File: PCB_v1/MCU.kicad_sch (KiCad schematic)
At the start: 40 parts, among them J6 Conn_ARM_JTAG_SWD_10, SW9 SW_Push, U5 STM32F405RGTx, Y1 ASE-8MHz-L-C-T

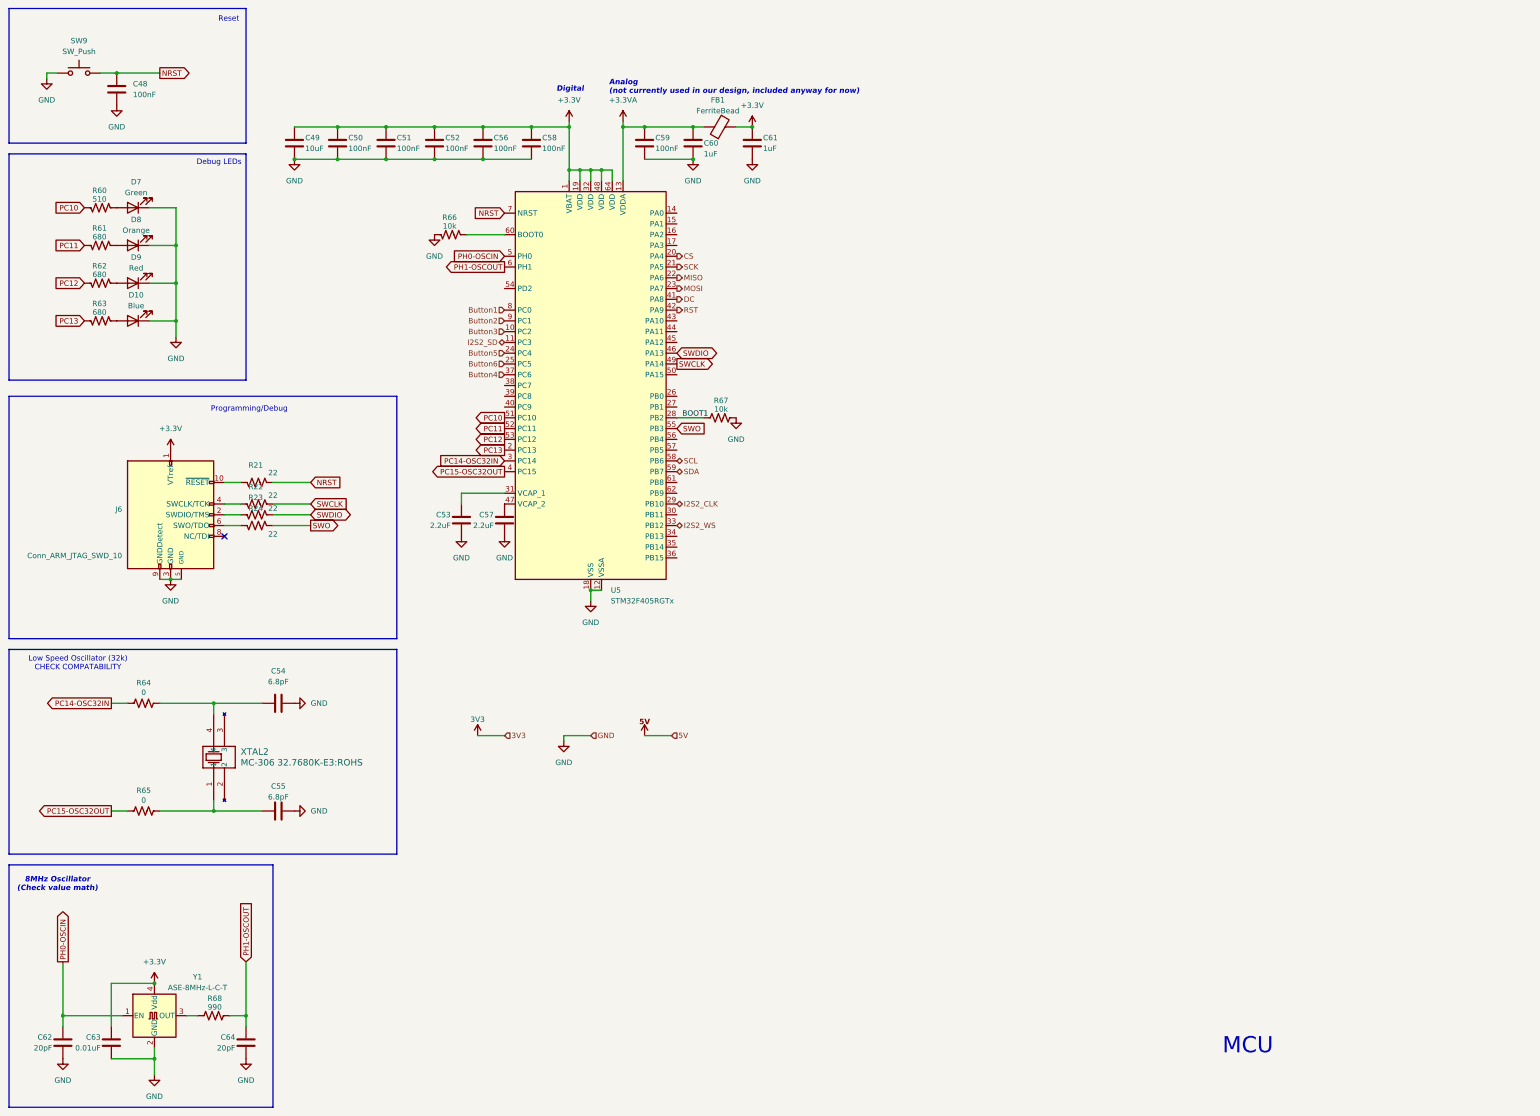
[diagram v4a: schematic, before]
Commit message: Update before adding AGND for the power delivery
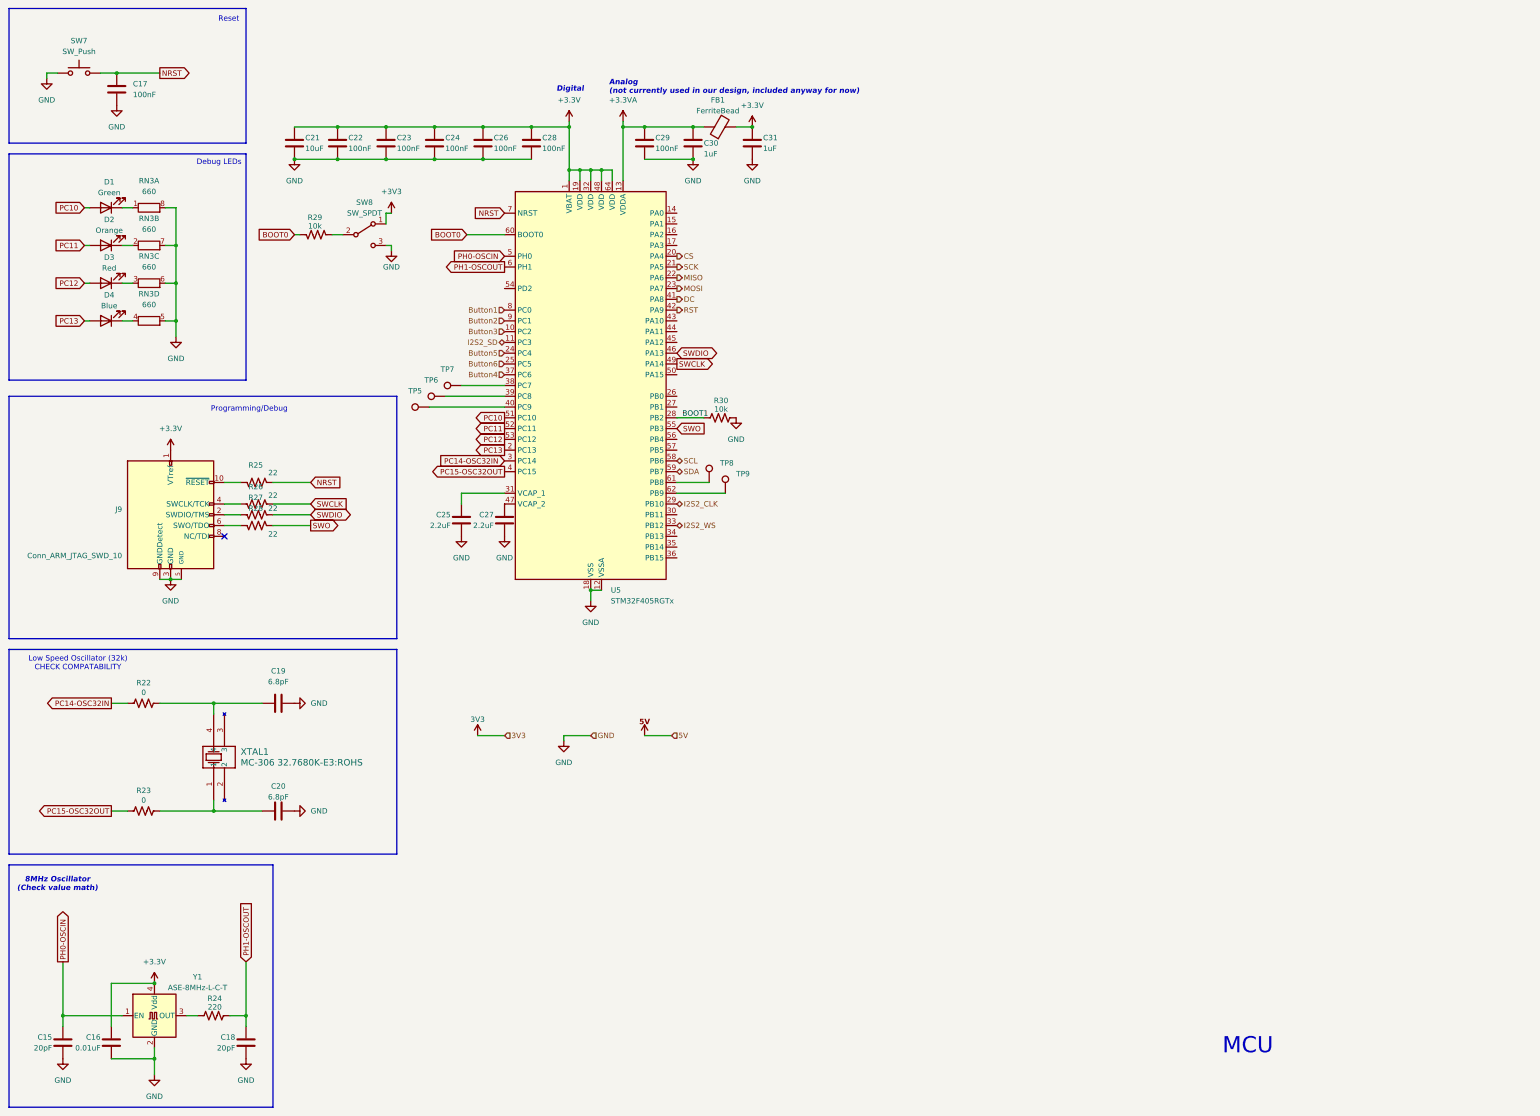
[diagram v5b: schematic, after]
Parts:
- removed R60: 510, Resistor_SMD:R_0805_2012Metric, symbol Device:R_US
- removed R61, R62, R63: 680, Resistor_SMD:R_0805_2012Metric, symbol Device:R_US
- removed R66: 10k, Resistor_SMD:R_0805_2012Metric, symbol Device:R_US
- added R29: 10k, Resistor_SMD:R_0805_2012Metric, symbol Device:R_US
- added RN3: 660, symbol Device:R_Pack04_Split
- added SW8: SW_SPDT, Button_Switch_SMD:SW_SPDT_PCM12, symbol Switch:SW_SPDT
- added TP5, TP6, TP7, TP8, TP9: ~, TestPoint:TestPoint_THTPad_D1.0mm_Drill0.5mm, symbol Connector:TestPoint
- R24: renamed from R68; value 990 -> 220
- renumbered C62 to C15, C63 to C16, C48 to C17, C64 to C18, C54 to C19, C55 to C20, C49 to C21, C50 to C22, C51 to C23, C52 to C24, C53 to C25, C56 to C26, C57 to C27, C58 to C28, C59 to C29, C60 to C30, C61 to C31, D7 to D1, D8 to D2, D9 to D3, D10 to D4, J6 to J9, R64 to R22, R65 to R23, R21 to R25, R22 to R26, R23 to R27, R24 to R28, R67 to R30, SW9 to SW7, XTAL2 to XTAL1
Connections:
- net GND: now also RN3.5 (R4.2), RN3.6 (R3.2), RN3.7 (R2.2), RN3.8 (R1.2), SW8.3 (C); no longer D1.1 (K), D2.1 (K), D3.1 (K), D4.1 (K)
- net PC10: now also D1.2 (A)
- net PC11: now also D2.2 (A)
- net PC12: now also D3.2 (A)
- net PC13: now also D4.2 (A)
- net BOOT0: now reaches U5.60 (BOOT0)
- net BOOT0: now also R29.2
- net at U5.38 (PC7): now also TP7.1
- net at U5.39 (PC8): now also TP6.1
- net at U5.40 (PC9): now also TP5.1
- net at U5.61 (PB8): now also TP8.1
- net at U5.62 (PB9): now also TP9.1
- new net: D3.1 (K), RN3.3 (R3.1)
- new net: D2.1 (K), RN3.2 (R2.1)
- new net: D1.1 (K), RN3.1 (R1.1)
- new net: R29.1, SW8.2 (B)
- new net: D4.1 (K), RN3.4 (R4.1)
- new net +3V3: SW8.1 (A)
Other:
- moved on the sheet: D1, D2, D3, D4

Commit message: Initial placement draft
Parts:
- removed R22, R23: 0, Resistor_SMD:R_0805_2012Metric, symbol Device:R_US
- added J1: Conn_01x03, Connector_PinHeader_2.54mm:PinHeader_1x03_P2.54mm_Vertical, symbol Connector_Generic:Conn_01x03
- added TP10, TP13: ~, TestPoint:TestPoint_THTPad_D1.0mm_Drill0.5mm, symbol Connector:TestPoint
- RN3: footprint (none) -> Parts_Library:RESCAXS80P320X160X60-8N; MFP (none) -> EXB-38V681JV
- SW8: renamed from SW7; footprint Button_Switch_SMD:SW_Push_1P1T_NO_CK_PTS125Sx43PSMTR -> SW_TS04-66-65-BK-160-SMT
- XTAL1: footprint MC_306_32_7680K_E3_ROHS:SO4_MC-306_SEC -> Parts_Library:SO4_MC-306_SEC
- renumbered D1 to D2, D2 to D3, D3 to D4, D4 to D5, SW8 to SW9, TP8 to TP11, TP9 to TP12, TP5 to TP7, TP6 to TP8, TP7 to TP9
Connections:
- net GND: now also J1.3 (Pin_3)
- net PC14-OSC32IN: now also C19.1, XTAL1.4, TP10.1
- net PC15-OSC32OUT: now also C20.1, XTAL1.1, TP13.1
- net STEP: now reaches U5.14 (PA0)
- net DIR: now reaches U5.15 (PA1)
- net MCU_TX: now reaches U5.16 (PA2)
- net MCU_TX: now also J1.2 (Pin_2)
- net MCU_RX: now reaches U5.17 (PA3)
- net MCU_RX: now also J1.1 (Pin_1)
- net PB4: now reaches U5.56 (PB4)
- net PB4: now also D5.2 (A)
- net PC13: no longer names the net of U5.2 (PC13)
- net PC13: no longer D5.2 (A)

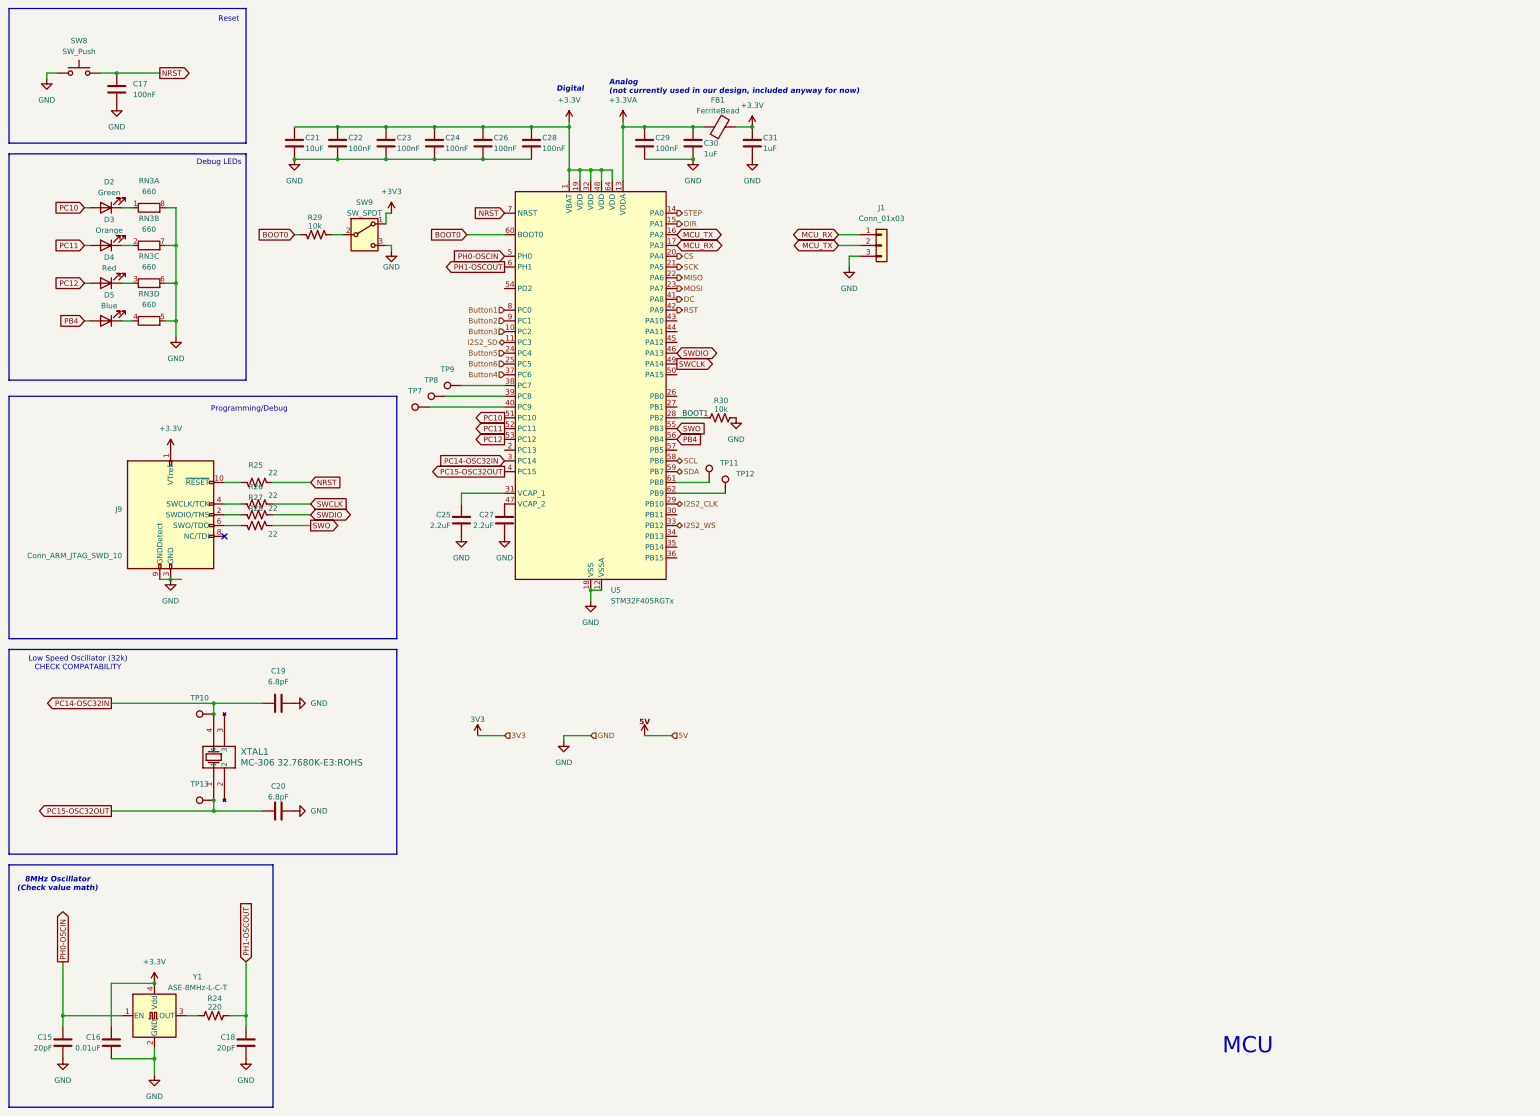
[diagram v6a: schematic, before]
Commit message: adjusted placments
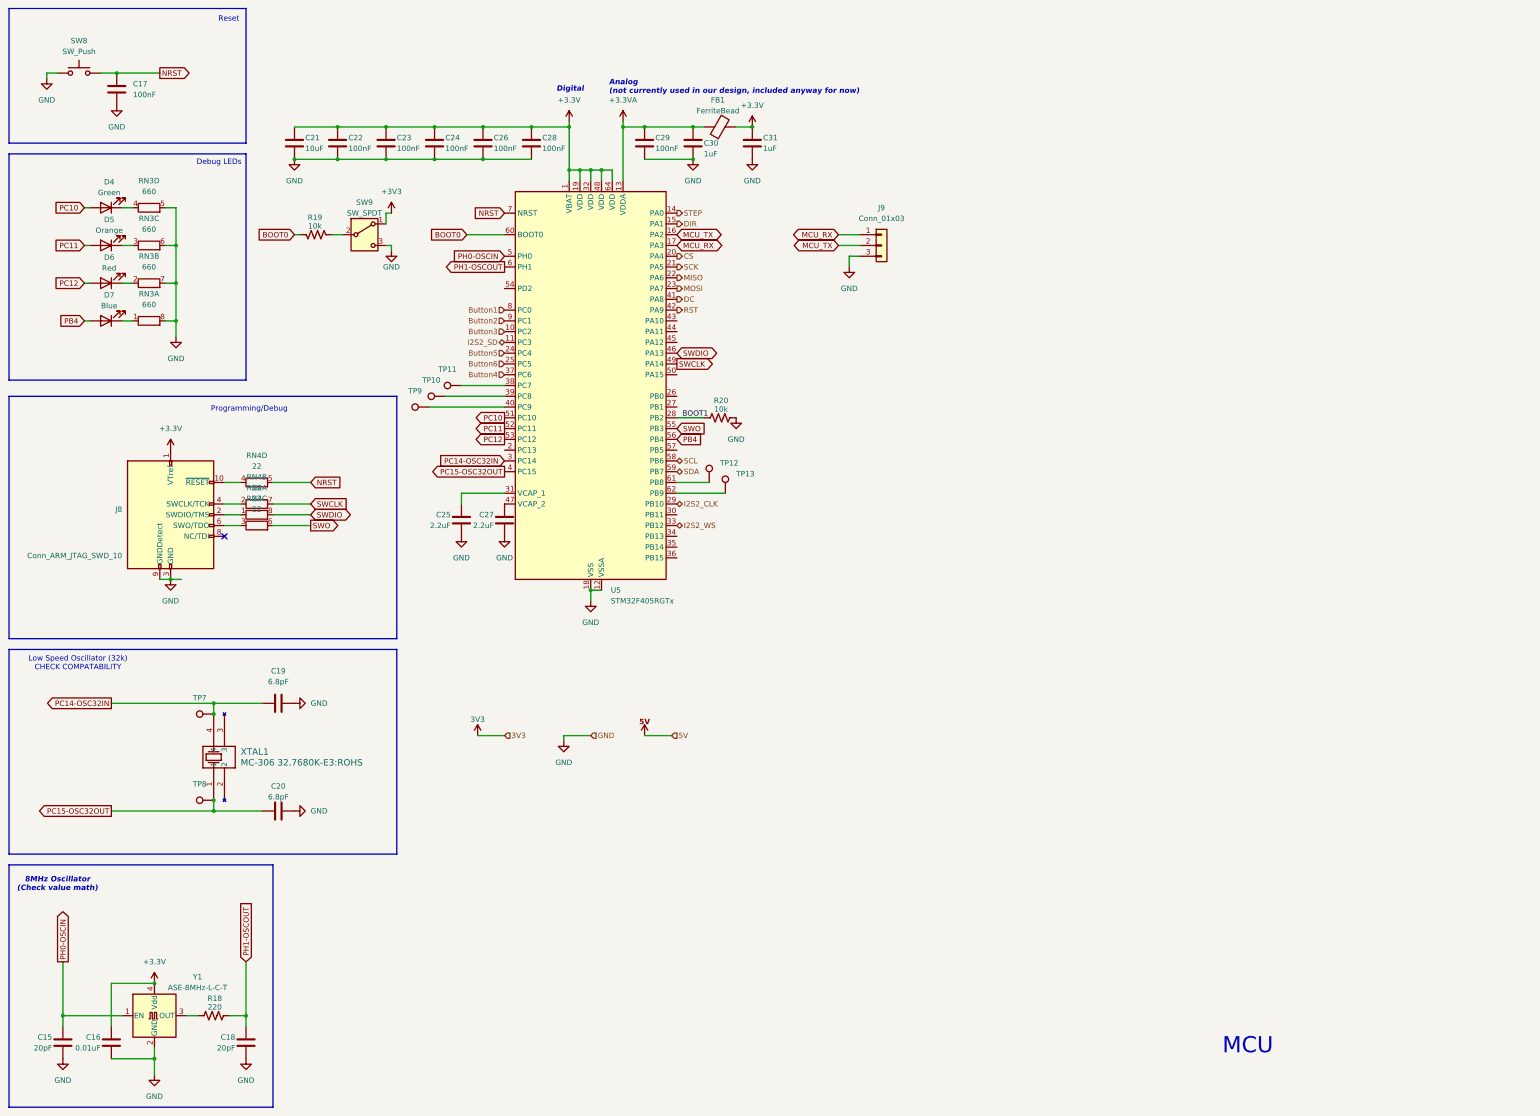
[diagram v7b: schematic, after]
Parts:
- removed R25, R26, R27, R28: 22, Resistor_SMD:R_0805_2012Metric, symbol Device:R_US
- added RN4: 22, Parts_Library:RESCAXE80P320X160X70-8N, symbol Device:R_Pack04_Split
- renumbered D2 to D4, D3 to D5, D4 to D6, D5 to D7, J9 to J8, J1 to J9, R24 to R18, R29 to R19, R30 to R20, TP8 to TP10, TP9 to TP11, TP11 to TP12, TP12 to TP13, TP10 to TP7, TP13 to TP8, TP7 to TP9
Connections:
- net NRST: now also RN4.5 (R4.2)
- net SWCLK: now also RN4.7 (R2.2)
- net SWDIO: now also RN4.8 (R1.2)
- net SWO: now also RN4.6 (R3.2)
- net at D6.1 (K): now also RN3.2 (R2.1); no longer RN3.3 (R3.1)
- net at D5.1 (K): now also RN3.3 (R3.1); no longer RN3.2 (R2.1)
- net at RN3.1 (R1.1): now also D7.1 (K); no longer D4.1 (K)
- net at J8.10 (~{RESET}): now also RN4.4 (R4.1)
- net at J8.2 (SWDIO/TMS): now also RN4.1 (R1.1)
- net at J8.4 (SWCLK/TCK): now also RN4.2 (R2.1)
- net at J8.6 (SWO/TDO): now also RN4.3 (R3.1)
- net at RN3.4 (R4.1): now also D4.1 (K); no longer D7.1 (K)

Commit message: Power Layout done
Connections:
- net +3V3 is gone; now on net +3.3V: SW9.1 (A)
- net BAT_EMPTY: now reaches U5.43 (PA10)
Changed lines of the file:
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@@
 	)
 	(junction
+		(at 130.81 187.96)
+		(diameter 0)
+		(color 0 0 0 0)
+	)
+	(junction
 		(at 177.8 44.45)
 		(diameter 0)
@@
 	)
 	(junction
+		(at 127 187.96)
+		(diameter 0)
+		(color 0 0 0 0)
+	)
+	(junction
 		(at 161.29 44.45)
 		(diameter 0)
@@
 	(wire
 		(pts
+			(xy 130.81 187.96) (xy 133.35 187.96)
+		)
+		(stroke
+			(width 0)
+			(type default)
+		)
+	)
+	(wire
+		(pts
 			(xy 214.63 74.93) (xy 217.17 74.93)
 		)
@@
 	(wire
 		(pts
+			(xy 127 187.96) (xy 130.81 187.96)
+		)
+		(stroke
+			(width 0)
+			(type default)
+		)
+	)
+	(wire
+		(pts
 			(xy 25.4 31.75) (xy 25.4 33.02)
 		)
@@
 	(wire
 		(pts
-			(xy 127 187.96) (xy 133.35 187.96)
+			(xy 119.38 187.96) (xy 127 187.96)
 		)
 		(stroke
@@
 		)
 	)
+	(hierarchical_label "BAT_EMPTY"
+		(shape input)
+		(at 173.99 90.17 0)
+		(effects
+			(font
+				(size 1.27 1.27)
+			)
+			(justify left)
+		)
+	)
 	(hierarchical_label "RST"
 		(shape output)
@@
 	(symbol
 		(lib_id "power:+3.3V")
+		(at 130.81 187.96 0)
+		(unit 1)
+		(exclude_from_sim no)
+		(in_bom yes)
+		(on_board yes)
+		(dnp no)
+		(fields_autoplaced yes)
+		(property "Reference" "#PWR0128"
+			(at 130.81 191.77 0)
+			(effects
+				(font
+					(size 1.27 1.27)
+				)
+				(hide yes)
+			)
+		)
+		(property "Value" "+3.3V"
+			(at 130.81 182.88 0)
+			(effects
+				(font
+					(size 1.27 1.27)
+				)
+			)
+		)
+		(property "Footprint" ""
+			(at 130.81 187.96 0)
+			(effects
+				(font
+					(size 1.27 1.27)
+				)
+				(hide yes)
+			)
+		)
+		(property "Datasheet" ""
+			(at 130.81 187.96 0)
+			(effects
+				(font
+					(size 1.27 1.27)
+				)
+				(hide yes)
+			)
+		)
+		(property "Description" "Power symbol creates a global label with name \"+3.3V\""
+			(at 130.81 187.96 0)
+			(effects
+				(font
+					(size 1.27 1.27)
+				)
+				(hide yes)
+			)
+		)
+		(pin "1"
+		)
+		(instances
+			(project "tuner time"
+				(path "/353cef6a-fb6e-40d9-89f8-eb54b7aa5118/d0611583-1674-4868-b9e4-3555a93f9ff1"
+					(reference "#PWR0128")
+					(unit 1)
+				)
+			)
+		)
+	)
+	(symbol
+		(lib_id "power:+3.3V")
 		(at 148.59 43.18 0)
 		(unit 1)
@@
 	)
 	(symbol
+		(lib_id "power:VCC")
+		(at 127 187.96 0)
+		(unit 1)
+		(exclude_from_sim no)
+		(in_bom yes)
+		(on_board yes)
+		(dnp no)
+		(property "Reference" "#PWR0127"
+			(at 127 191.77 0)
+			(effects
+				(font
+					(size 1.27 1.27)
+				)
+				(hide yes)
+			)
+		)
+		(property "Value" "3V3"
+			(at 127 184.15 0)
+			(effects
+				(font
+					(size 1.27 1.27)
+				)
+			)
+		)
+		(property "Footprint" ""
+			(at 127 187.96 0)
+			(effects
+				(font
+					(size 1.27 1.27)
+				)
+				(hide yes)
+			)
+		)
+		(property "Datasheet" ""
+			(at 127 187.96 0)
+			(effects
+				(font
+					(size 1.27 1.27)
+				)
+				(hide yes)
+			)
+		)
+		(property "Description" "Power symbol creates a global label with name \"VCC\""
+			(at 127 187.96 0)
+			(effects
+				(font
+					(size 1.27 1.27)
+				)
+				(hide yes)
+			)
+		)
+		(pin "1"
+		)
+		(instances
+			(project "tuner time"
+				(path "/353cef6a-fb6e-40d9-89f8-eb54b7aa5118/d0611583-1674-4868-b9e4-3555a93f9ff1"
+					(reference "#PWR0127")
+					(unit 1)
+				)
+			)
+		)
+	)
+	(symbol
 		(lib_id "Connector:TestPoint")
 		(at 181.61 128.27 0)
@@
 	(symbol
 		(lib_id "power:VCC")
-		(at 127 187.96 0)
+		(at 119.38 187.96 0)
 		(unit 1)
 		(exclude_from_sim no)
@@
 		(dnp no)
 		(property "Reference" "#PWR0101"
-			(at 127 191.77 0)
+			(at 119.38 191.77 0)
 			(effects
 				(font
@@
 			)
 		)
-		(property "Value" "3V3"
-			(at 127 184.15 0)
+		(property "Value" "+3V3"
+			(at 119.38 184.15 0)
 			(effects
 				(font
@@
 		)
 		(property "Footprint" ""
-			(at 127 187.96 0)
+			(at 119.38 187.96 0)
 			(effects
 				(font
@@
 		)
 		(property "Datasheet" ""
-			(at 127 187.96 0)
+			(at 119.38 187.96 0)
 			(effects
 				(font
@@
 		)
 		(property "Description" "Power symbol creates a global label with name \"VCC\""
-			(at 127 187.96 0)
+			(at 119.38 187.96 0)
 			(effects
 				(font
